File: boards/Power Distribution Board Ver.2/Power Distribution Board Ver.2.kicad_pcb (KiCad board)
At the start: 4 copper layers, 127 x 127 mm, 95 parts, among them J1 Screw_Terminal_01x02, J2 Screw_Terminal_01x06, J3 Screw_Terminal_01x06, J4 Screw_Terminal_01x06, K1 Relay, K2 Relay, K3 Relay, K4 Relay, K5 Relay, K6 Relay, SW1 SW_Push_Open, U1 SIC431AED-T1-GE3, U2 SIC431AED-T1-GE3, U3 SIC431AED-T1-GE3

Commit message: Fix labeling
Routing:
- net Net-(D7-A): track 47.1 -> 56.0 mm
- net Net-(D9-A): track 52.0 -> 60.4 mm
- net Net-(D8-A): track 56.6 -> 63.9 mm
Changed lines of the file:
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@@
   (segment (start 32.436345 74.4075) (end 32.453845 74.39) (width 0.9) (layer "F.Cu") (net 14))
   (segment (start 30.233845 74.4075) (end 32.436345 74.4075) (width 0.9) (layer "F.Cu") (net 14))
+  (segment (start 70.548845 89.85) (end 70.548845 89.947792) (width 0.9) (layer "F.Cu") (net 15))
   (segment (start 74.575765 106.975) (end 75.833845 105.71692) (width 2) (layer "F.Cu") (net 15))
   (segment (start 67.753845 119.07) (end 67.753845 115.82) (width 0.9) (layer "F.Cu") (net 15))
   (segment (start 70.548845 89.85) (end 70.548845 88.6225) (width 0.9) (layer "F.Cu") (net 15))
+  (segment (start 75.241053 94.64) (end 75.833845 94.64) (width 0.9) (layer "F.Cu") (net 15))
   (segment (start 75.833845 108.48615) (end 75.833845 108.23308) (width 2) (layer "F.Cu") (net 15))
   (segment (start 74.575765 106.975) (end 75.340765 107.74) (width 0.9) (layer "F.Cu") (net 15))
   (segment (start 66.803845 106.975) (end 74.575765 106.975) (width 2) (layer "F.Cu") (net 15))
+  (segment (start 70.548845 89.947792) (end 75.241053 94.64) (width 0.9) (layer "F.Cu") (net 15))
   (segment (start 68.323845 86.04) (end 67.966345 86.04) (width 0.2) (layer "F.Cu") (net 15))
   (segment (start 69.778345 84.5855) (end 68.323845 86.04) (width 0.2) (layer "F.Cu") (net 15))
@@
   (segment (start 69.778345 82.587) (end 69.778345 84.5855) (width 0.2) (layer "F.Cu") (net 15))
   (segment (start 55.053845 119.07) (end 55.053845 111.71538) (width 0.9) (layer "F.Cu") (net 16))
+  (segment (start 54.286053 94.64) (end 55.513845 94.64) (width 0.9) (layer "F.Cu") (net 16))
   (segment (start 46.126345 79.895) (end 48.188345 81.957) (width 0.2) (layer "F.Cu") (net 16))
   (segment (start 48.958845 88.6225) (end 48.958845 89.215) (width 0.9) (layer "F.Cu") (net 16))
   (segment (start 54.235765 106.995) (end 55.513845 105.71692) (width 2) (layer "F.Cu") (net 16))
   (segment (start 46.884345 86.548) (end 48.958845 88.6225) (width 0.9) (layer "F.Cu") (net 16))
+  (segment (start 48.958845 89.215) (end 48.958845 89.312792) (width 0.9) (layer "F.Cu") (net 16))
   (segment (start 47.12 106.995) (end 54.235765 106.995) (width 2) (layer "F.Cu") (net 16))
   (segment (start 54.235765 106.995) (end 55.053845 107.81308) (width 2) (layer "F.Cu") (net 16))
@@
   (segment (start 46.376345 86.548) (end 46.884345 86.548) (width 0.9) (layer "F.Cu") (net 16))
   (segment (start 55.513845 111.25538) (end 55.513845 94.64) (width 2) (layer "F.Cu") (net 16))
+  (segment (start 48.958845 89.312792) (end 54.286053 94.64) (width 0.9) (layer "F.Cu") (net 16))
   (segment (start 48.188345 81.957) (end 48.188345 84.94045) (width 0.2) (layer "F.Cu") (net 16))
   (segment (start 46.580795 86.548) (end 46.376345 86.548) (width 0.2) (layer "F.Cu") (net 16))
+  (segment (start 30.783845 90.427792) (end 34.996053 94.64) (width 0.9) (layer "F.Cu") (net 17))
   (segment (start 36.055765 106.995) (end 36.698845 106.995) (width 2) (layer "F.Cu") (net 17))
   (segment (start 30.783845 90.33) (end 29.966345 90.33) (width 0.9) (layer "F.Cu") (net 17))
@@
   (segment (start 42.353845 119.07) (end 42.353845 117.22) (width 0.9) (layer "F.Cu") (net 17))
   (segment (start 28.703845 106.995) (end 36.055765 106.995) (width 2) (layer "F.Cu") (net 17))
+  (segment (start 34.996053 94.64) (end 37.333845 94.64) (width 0.9) (layer "F.Cu") (net 17))
+  (segment (start 30.783845 90.33) (end 30.783845 90.427792) (width 0.9) (layer "F.Cu") (net 17))
   (segment (start 42.353845 117.22) (end 37.333845 112.2) (width 0.9) (layer "F.Cu") (net 17))
   (segment (start 28.581345 79.895) (end 28.581345 86.635) (width 0.2) (layer "F.Cu") (net 17))

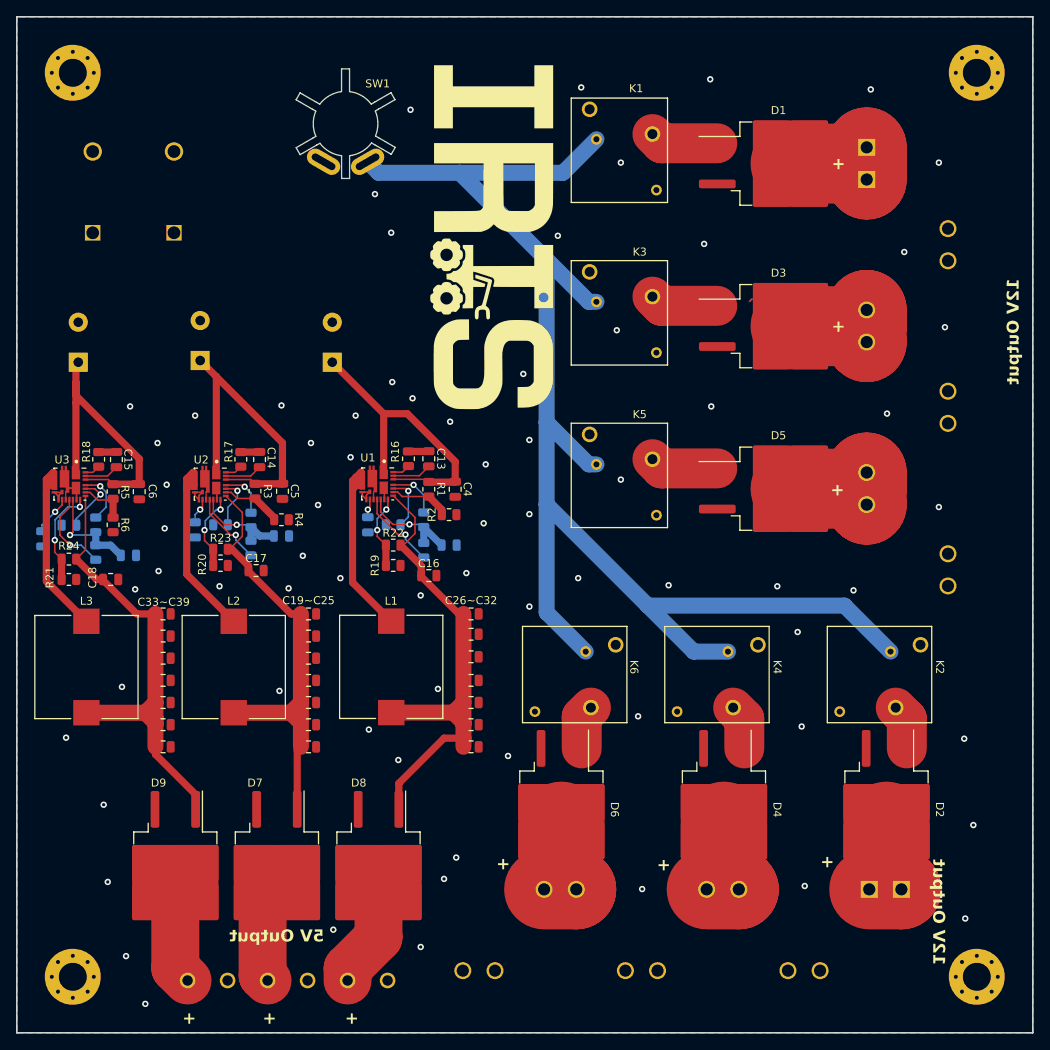
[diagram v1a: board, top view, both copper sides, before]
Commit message: minor front silkscreen change
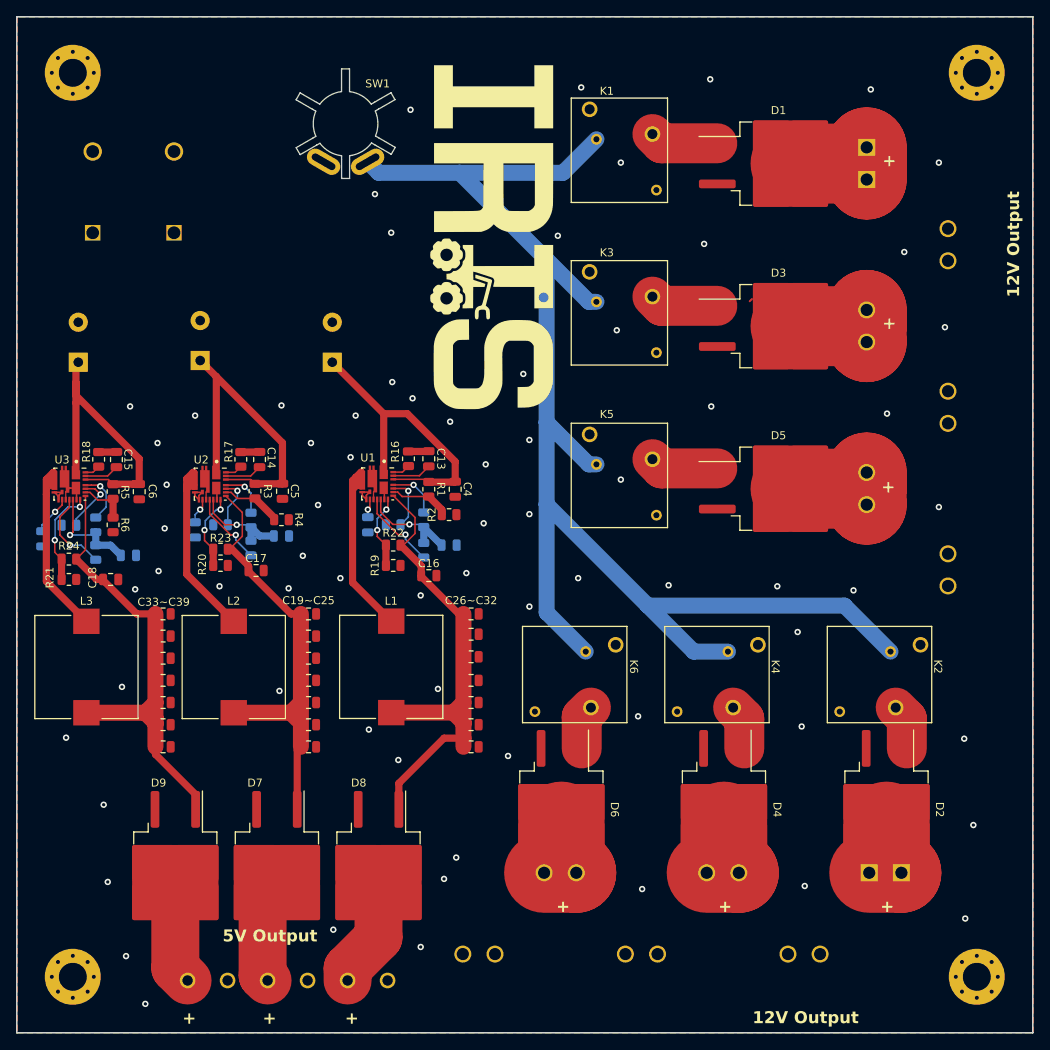
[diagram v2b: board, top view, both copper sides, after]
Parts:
- moved J3 2.07 mm to (130.6, 127.0)
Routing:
- net /12V_IN_6: track 13.3 -> 11.2 mm
- net /12V_IN_5: track 13.3 -> 11.2 mm
- net /12V_IN_4: track 13.3 -> 11.2 mm

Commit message: Names Update
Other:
- board text added: "IRIS - XV PROBEPCBPCB Ver. 2 Buffett Lee, Emily Lory, Joseph Hanger Nathan Colunga, Miaomiao Jin, Henry Lin Ben Saarva, Wyatt Sturn, Jakub Wojdyla"
- board text removed: "IRIS - XV PROBEPCBPCB Ver. 2 Buffett Lee, Emily Lory, Joseph Hanger, Henry Lin Nathan Colunga, Ben Saarva, Jakub Wojdyla Wyatt Sturn, Miaomiao Jin"
